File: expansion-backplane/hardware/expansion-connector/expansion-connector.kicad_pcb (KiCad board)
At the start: 2 copper layers, 39 x 45 mm, 2 parts

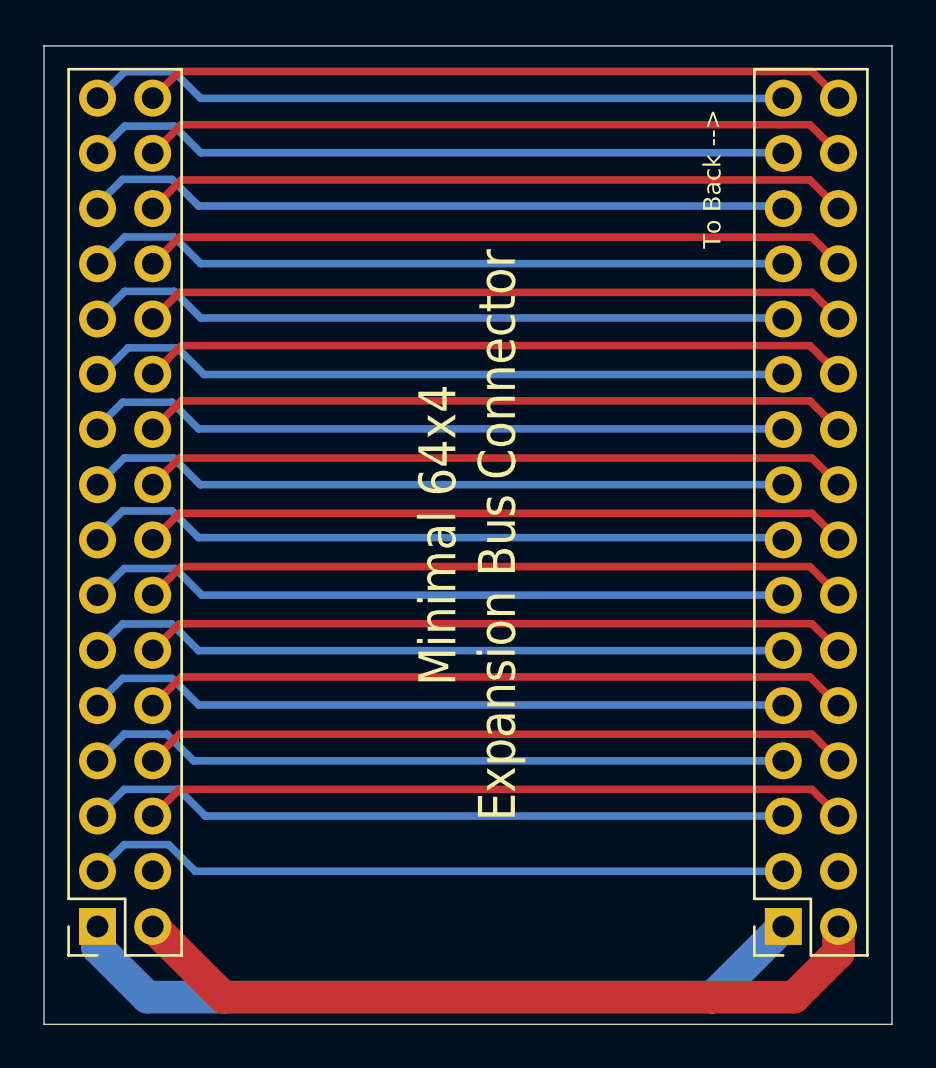
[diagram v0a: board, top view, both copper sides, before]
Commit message: added better ground plane
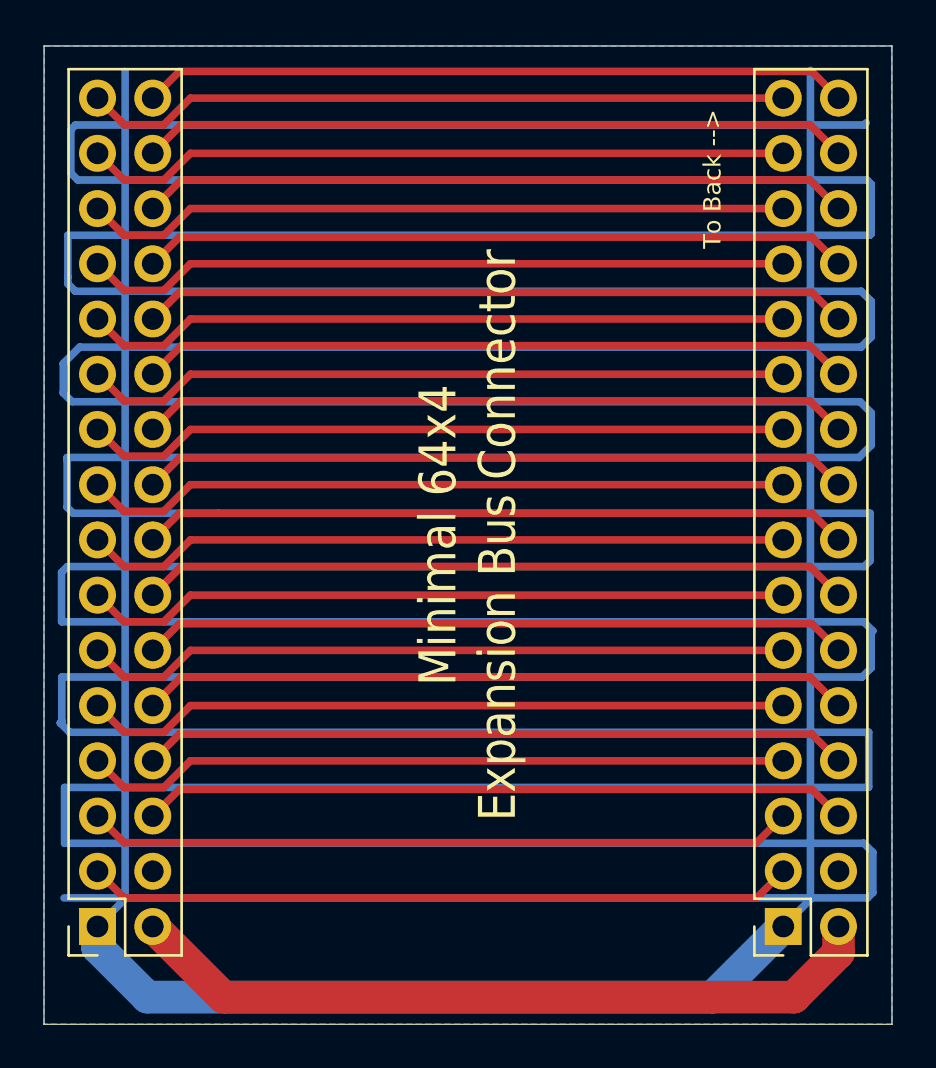
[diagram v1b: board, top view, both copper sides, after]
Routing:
- net GND: track 34.8 -> 701.8 mm
- added copper zone on B.Cu, net GND
